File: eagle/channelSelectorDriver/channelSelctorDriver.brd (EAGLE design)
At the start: 10 parts, among them IC1 4025N, IC2 4071N, IC3 4071N

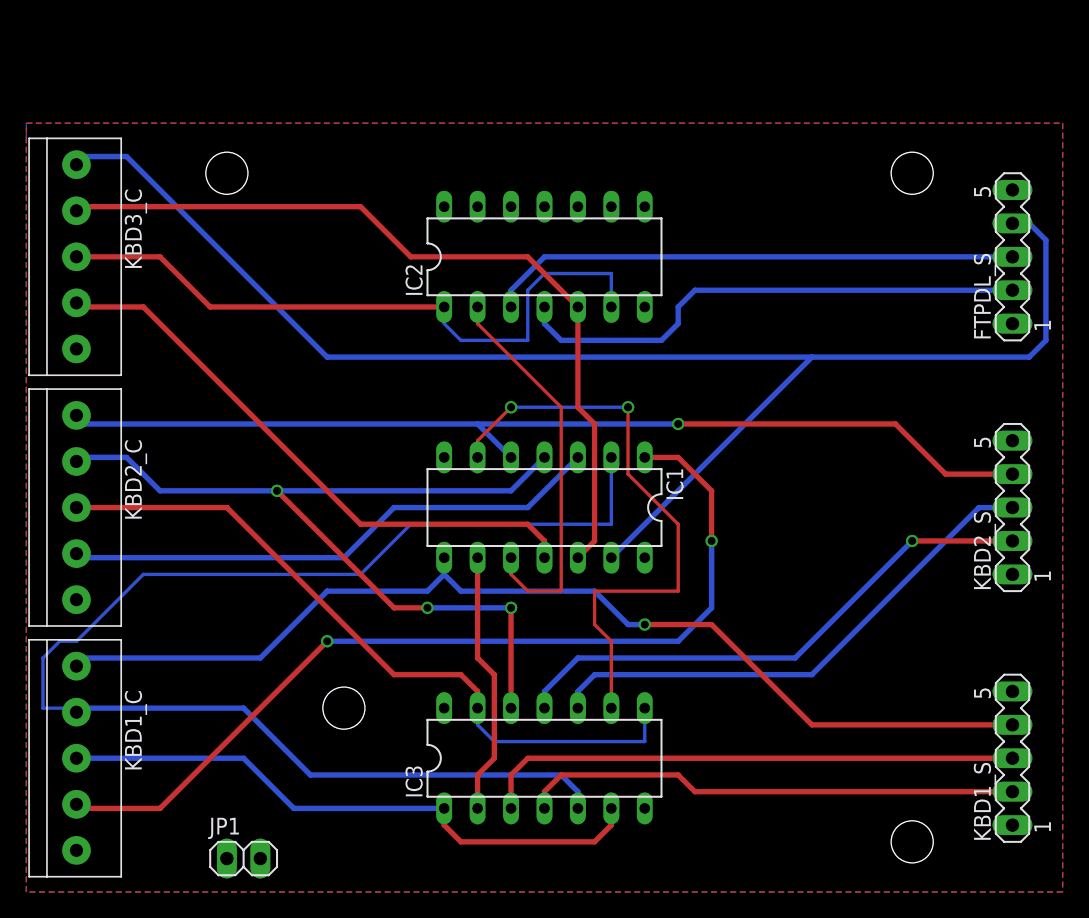
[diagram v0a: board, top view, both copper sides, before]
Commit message: Added labels to channel selector driver
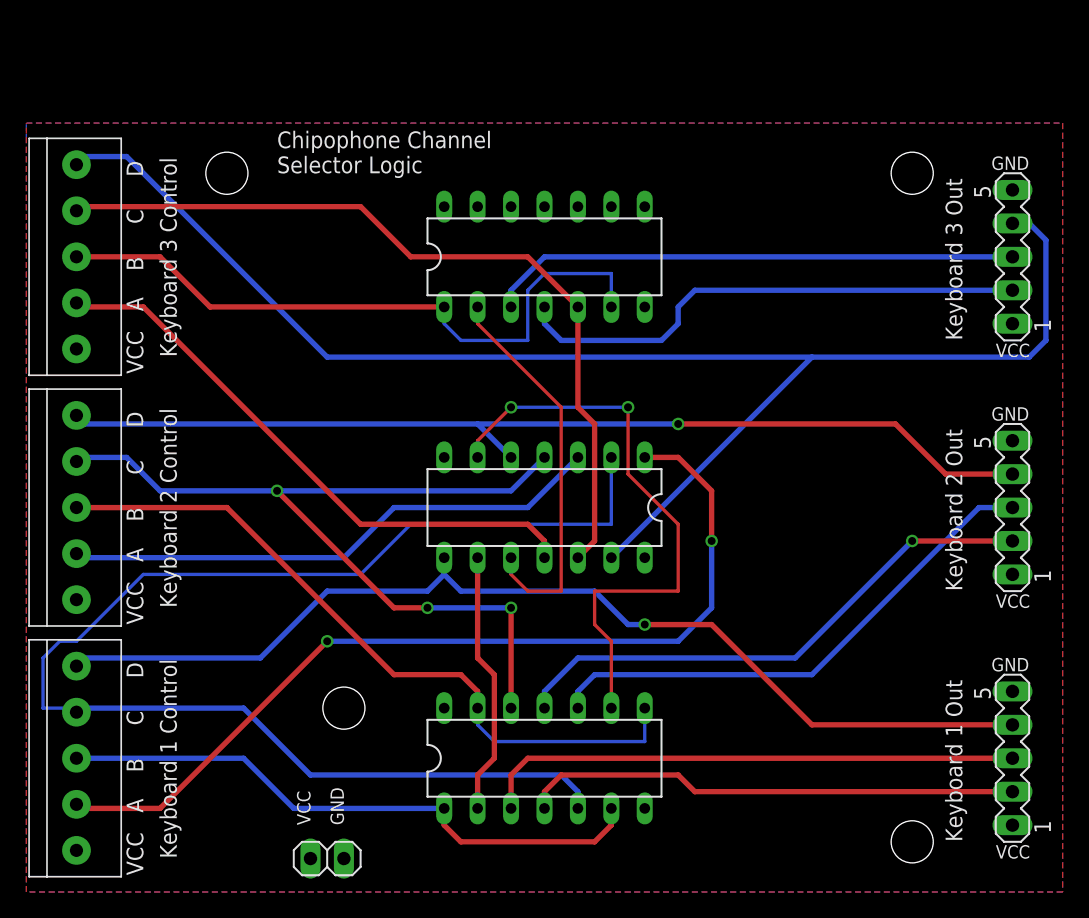
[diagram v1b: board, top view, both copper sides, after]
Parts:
- moved JP1 6.35 mm to (22.9, 2.54)
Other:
- board text added: "Chipophone Channel Selector Logic"
- board text added: "GND"
- board text added: "Keyboard 1 Control"
- board text added: "Keyboard 1 Out"
- board text added: "Keyboard 2 Control"
- board text added: "Keyboard 2 Out"
- board text added: "Keyboard 3 Control"
- board text added: "Keyboard 3 Out"
- board text added: "VCC"
- board text added: "VCC A B C D"
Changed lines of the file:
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@@
 <hole x="67.31" y="54.61" drill="3.2"/>
 <hole x="24.13" y="13.97" drill="3.2"/>
+<text x="21.59" y="5.08" size="1.016" layer="25" rot="R90">VCC</text>
+<text x="24.13" y="5.08" size="1.016" layer="25" rot="R90">GND</text>
+<text x="11.43" y="2.54" size="1.27" layer="25" rot="R90">Keyboard 1 Control</text>
+<text x="11.43" y="21.59" size="1.27" layer="25" rot="R90">Keyboard 2 Control</text>
+<text x="11.43" y="40.64" size="1.27" layer="25" rot="R90">Keyboard 3 Control</text>
+<text x="73.66" y="40.64" size="1.016" layer="25">VCC</text>
+<text x="73.66" y="21.59" size="1.016" layer="25">VCC</text>
+<text x="73.66" y="2.54" size="1.016" layer="25">VCC</text>
+<text x="76.2" y="17.78" size="1.016" layer="25" rot="R180">GND</text>
+<text x="76.2" y="36.83" size="1.016" layer="25" rot="R180">GND</text>
+<text x="76.2" y="55.88" size="1.016" layer="25" rot="R180">GND</text>
+<text x="71.12" y="41.91" size="1.27" layer="25" rot="R90">Keyboard 3 Out</text>
+<text x="71.12" y="22.86" size="1.27" layer="25" rot="R90">Keyboard 2 Out</text>
+<text x="71.12" y="3.81" size="1.27" layer="25" rot="R90">Keyboard 1 Out</text>
+<text x="8.89" y="1.27" size="1.27" layer="25" rot="R90">VCC   A    B     C     D</text>
+<text x="8.89" y="20.32" size="1.27" layer="25" rot="R90">VCC   A    B     C     D</text>
+<text x="8.89" y="39.37" size="1.27" layer="25" rot="R90">VCC   A    B     C     D</text>
+<text x="19.05" y="54.61" size="1.27" layer="25">Chipophone Channel
+Selector Logic</text>
 </plain>
 <attributes>
@@
 </autorouter>
 <elements>
-<element name="KBD1_S" library="con-lstb" package="MA05-1" value="" x="74.93" y="10.16" rot="R90">
+<element name="KBD1_S" library="con-lstb" package="MA05-1" value="" x="74.93" y="10.16" smashed="yes" rot="R90">
 <attribute name="OC_NEWARK" value="unknown" x="74.93" y="10.16" size="1.778" layer="27" rot="R90" display="off"/>
 <attribute name="MPN" value="" x="74.93" y="10.16" size="1.778" layer="27" rot="R90" display="off"/>
 <attribute name="MF" value="" x="74.93" y="10.16" size="1.778" layer="27" rot="R90" display="off"/>
 <attribute name="OC_FARNELL" value="unknown" x="74.93" y="10.16" size="1.778" layer="27" rot="R90" display="off"/>
-</element>
-<element name="KBD2_S" library="con-lstb" package="MA05-1" value="" x="74.93" y="29.21" rot="R90">
+<attribute name="VALUE" x="77.851" y="7.62" size="1.27" layer="27" ratio="10" rot="R90"/>
+</element>
+<element name="KBD2_S" library="con-lstb" package="MA05-1" value="" x="74.93" y="29.21" smashed="yes" rot="R90">
 <attribute name="OC_NEWARK" value="unknown" x="74.93" y="29.21" size="1.778" layer="27" rot="R90" display="off"/>
 <attribute name="MPN" value="" x="74.93" y="29.21" size="1.778" layer="27" rot="R90" display="off"/>
 <attribute name="MF" value="" x="74.93" y="29.21" size="1.778" layer="27" rot="R90" display="off"/>
 <attribute name="OC_FARNELL" value="unknown" x="74.93" y="29.21" size="1.778" layer="27" rot="R90" display="off"/>
-</element>
-<element name="FTPDL_S" library="con-lstb" package="MA05-1" value="" x="74.93" y="48.26" rot="R90">
+<attribute name="VALUE" x="77.851" y="26.67" size="1.27" layer="27" ratio="10" rot="R90"/>
+</element>
+<element name="FTPDL_S" library="con-lstb" package="MA05-1" value="" x="74.93" y="48.26" smashed="yes" rot="R90">
 <attribute name="OC_NEWARK" value="unknown" x="74.93" y="48.26" size="1.778" layer="27" rot="R90" display="off"/>
 <attribute name="MPN" value="" x="74.93" y="48.26" size="1.778" layer="27" rot="R90" display="off"/>
 <attribute name="MF" value="" x="74.93" y="48.26" size="1.778" layer="27" rot="R90" display="off"/>
 <attribute name="OC_FARNELL" value="unknown" x="74.93" y="48.26" size="1.778" layer="27" rot="R90" display="off"/>
-</element>
-<element name="IC1" library="40xx" package="DIL14" value="4025N" x="39.37" y="29.21" rot="R180"/>
-<element name="IC2" library="40xx" package="DIL14" value="4071N" x="39.37" y="48.26"/>
-<element name="IC3" library="40xx" package="DIL14" value="4071N" x="39.37" y="10.16"/>
-<element name="JP1" library="pinhead" package="1X02" value="" x="16.51" y="2.54"/>
-<element name="KBD1_C" library="adafruit" package="1X05-3.5MM" value="1X5" x="3.81" y="10.16" rot="R270"/>
-<element name="KBD2_C" library="adafruit" package="1X05-3.5MM" value="1X5" x="3.81" y="29.21" rot="R270"/>
-<element name="KBD3_C" library="adafruit" package="1X05-3.5MM" value="1X5" x="3.81" y="48.26" rot="R270"/>
+<attribute name="VALUE" x="77.851" y="45.72" size="1.27" layer="27" ratio="10" rot="R90"/>
+</element>
+<element name="IC1" library="40xx" package="DIL14" value="4025N" x="39.37" y="29.21" smashed="yes" rot="R180">
+<attribute name="VALUE" x="46.101" y="29.845" size="1.27" layer="27" ratio="10" rot="R180"/>
+</element>
+<element name="IC2" library="40xx" package="DIL14" value="4071N" x="39.37" y="48.26" smashed="yes">
+<attribute name="VALUE" x="32.639" y="47.625" size="1.27" layer="27" ratio="10"/>
+</element>
+<element name="IC3" library="40xx" package="DIL14" value="4071N" x="39.37" y="10.16" smashed="yes">
+<attribute name="VALUE" x="32.639" y="9.525" size="1.27" layer="27" ratio="10"/>
+</element>
+<element name="JP1" library="pinhead" package="1X02" value="" x="22.86" y="2.54" smashed="yes">
+<attribute name="VALUE" x="20.32" y="-0.635" size="1.27" layer="27"/>
+</element>
+<element name="KBD1_C" library="adafruit" package="1X05-3.5MM" value="1X5" x="3.81" y="10.16" smashed="yes" rot="R270"/>
+<element name="KBD2_C" library="adafruit" package="1X05-3.5MM" value="1X5" x="3.81" y="29.21" smashed="yes" rot="R270"/>
+<element name="KBD3_C" library="adafruit" package="1X05-3.5MM" value="1X5" x="3.81" y="48.26" smashed="yes" rot="R270"/>
 </elements>
 <signals>
@@
 </board>
 </drawing>
+<compatibility>
+<note version="6.3" minversion="6.2.2" severity="warning">
+Since Version 6.2.2 text objects can contain more than one line,
+which will not be processed correctly with this version.
+</note>
+</compatibility>
 </eagle>
